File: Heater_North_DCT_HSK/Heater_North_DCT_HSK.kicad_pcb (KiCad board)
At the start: 2 copper layers, 52.1 x 57.1 mm, 8 parts, among them J1 NHB1, J2 NHB2, J3 Heater North

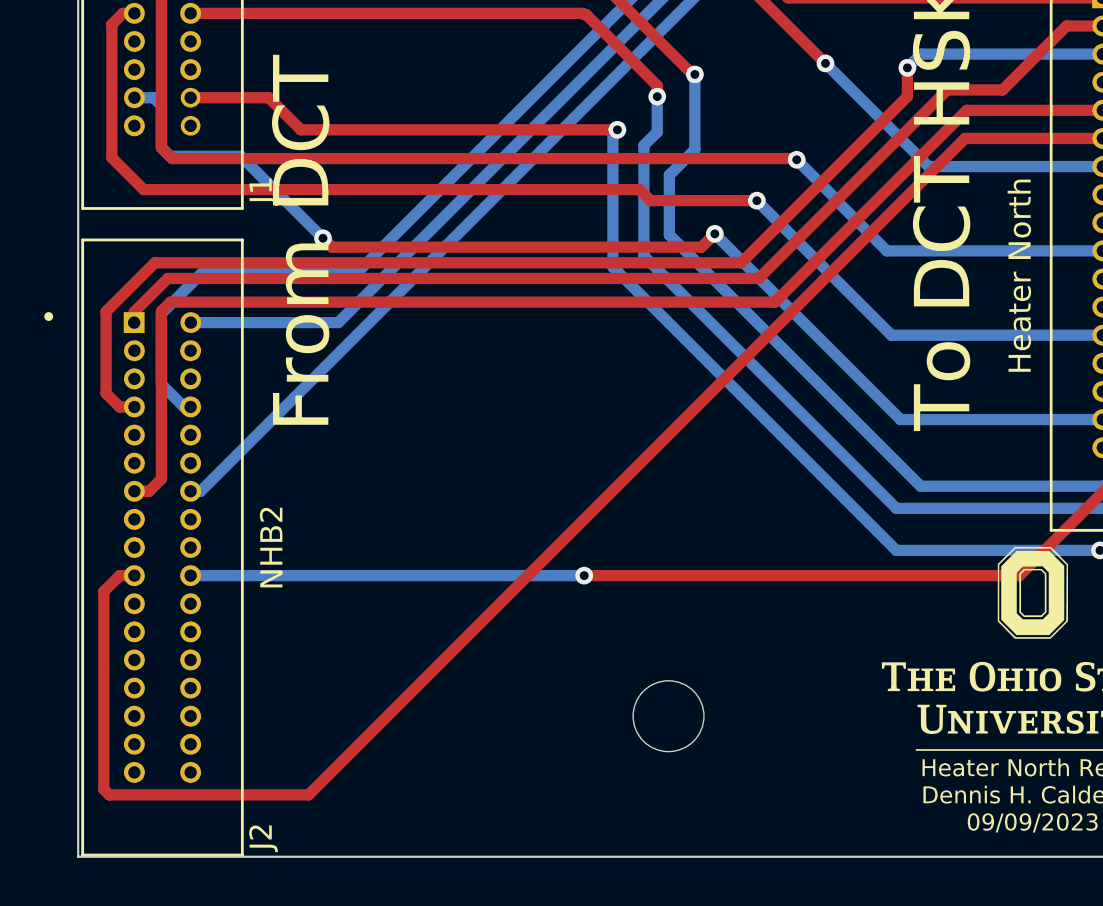
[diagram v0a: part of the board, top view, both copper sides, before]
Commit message: Updated Heater South with correct mapping referencing DCT_Heater_Driver schematic. Updated silscreen on all boards. Generated fabrication files.
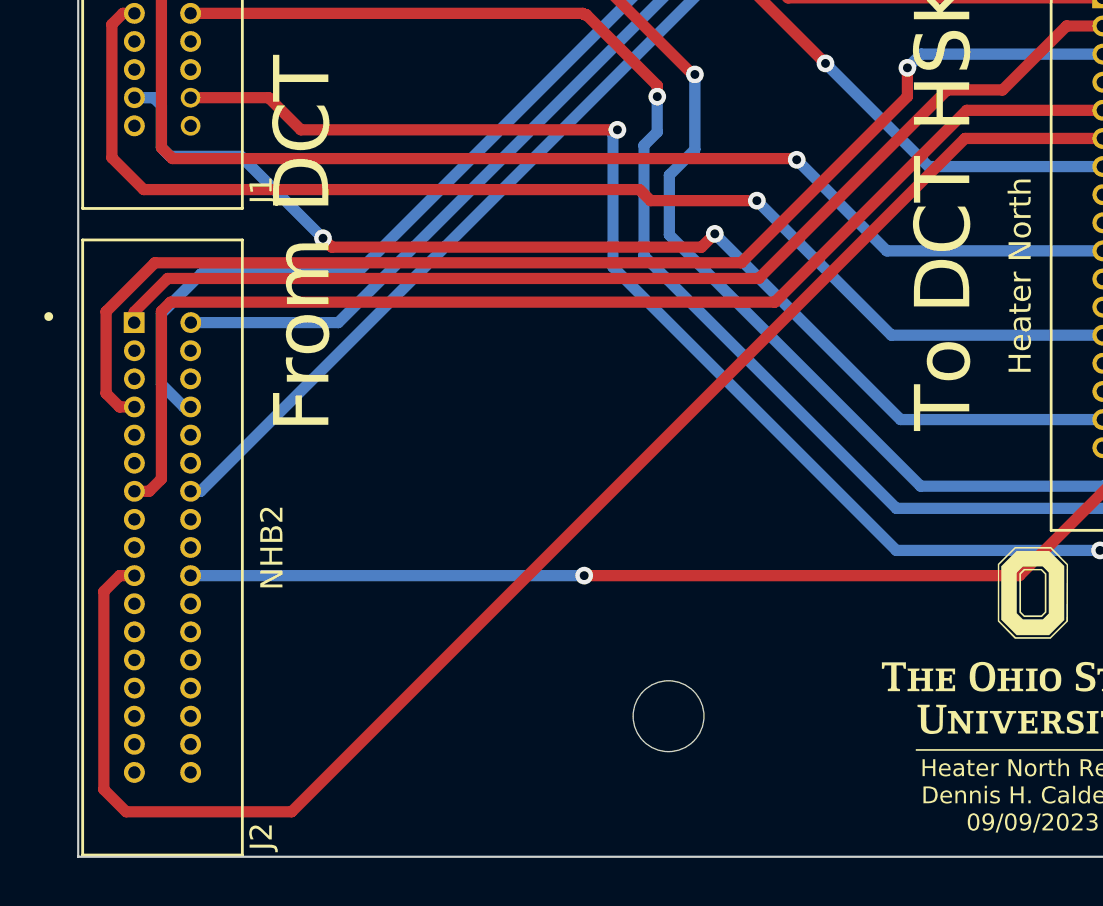
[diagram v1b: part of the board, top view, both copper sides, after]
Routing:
- net /HB2_19: track 68.1 -> 68.8 mm
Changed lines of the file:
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@@
       (outputformat 1)
       (mirror false)
-      (drillshape 1)
+      (drillshape 0)
       (scaleselection 1)
-      (outputdirectory "")
+      (outputdirectory "Fab/Rev_B")
     )
   )
@@
   (segment (start 139 69.6) (end 139 64.2) (width 0.508) (layer "B.Cu") (net 48))
   (segment (start 137.9 63.1) (end 121.5 63.1) (width 0.508) (layer "B.Cu") (net 48))
-  (segment (start 92.6 92.154754) (end 93.314754 91.44) (width 0.508) (layer "F.Cu") (net 53))
-  (segment (start 101.846261 101.346) (end 92.846 101.346) (width 0.508) (layer "F.Cu") (net 53))
-  (segment (start 93.314754 91.44) (end 93.98 91.44) (width 0.508) (layer "F.Cu") (net 53))
+  (segment (start 101.084261 102.108) (end 93.608 102.108) (width 0.508) (layer "F.Cu") (net 53))
   (segment (start 137.73 71.69) (end 131.502261 71.69) (width 0.508) (layer "F.Cu") (net 53))
+  (segment (start 131.502261 71.69) (end 101.084261 102.108) (width 0.508) (layer "F.Cu") (net 53))
+  (segment (start 93.314754 91.44) (end 93.98 91.44) (width 0.508) (layer "F.Cu") (net 53))
+  (segment (start 93.608 102.108) (end 92.6 101.1) (width 0.508) (layer "F.Cu") (net 53))
+  (segment (start 92.6 92.154754) (end 93.314754 91.44) (width 0.508) (layer "F.Cu") (net 53))
   (segment (start 92.6 101.1) (end 92.6 92.154754) (width 0.508) (layer "F.Cu") (net 53))
-  (segment (start 92.846 101.346) (end 92.6 101.1) (width 0.508) (layer "F.Cu") (net 53))
-  (segment (start 131.502261 71.69) (end 101.846261 101.346) (width 0.508) (layer "F.Cu") (net 53))
   (segment (start 139 86.4) (end 139 72.294754) (width 0.508) (layer "F.Cu") (net 54))
   (segment (start 114.3 91.44) (end 133.96 91.44) (width 0.508) (layer "F.Cu") (net 54))

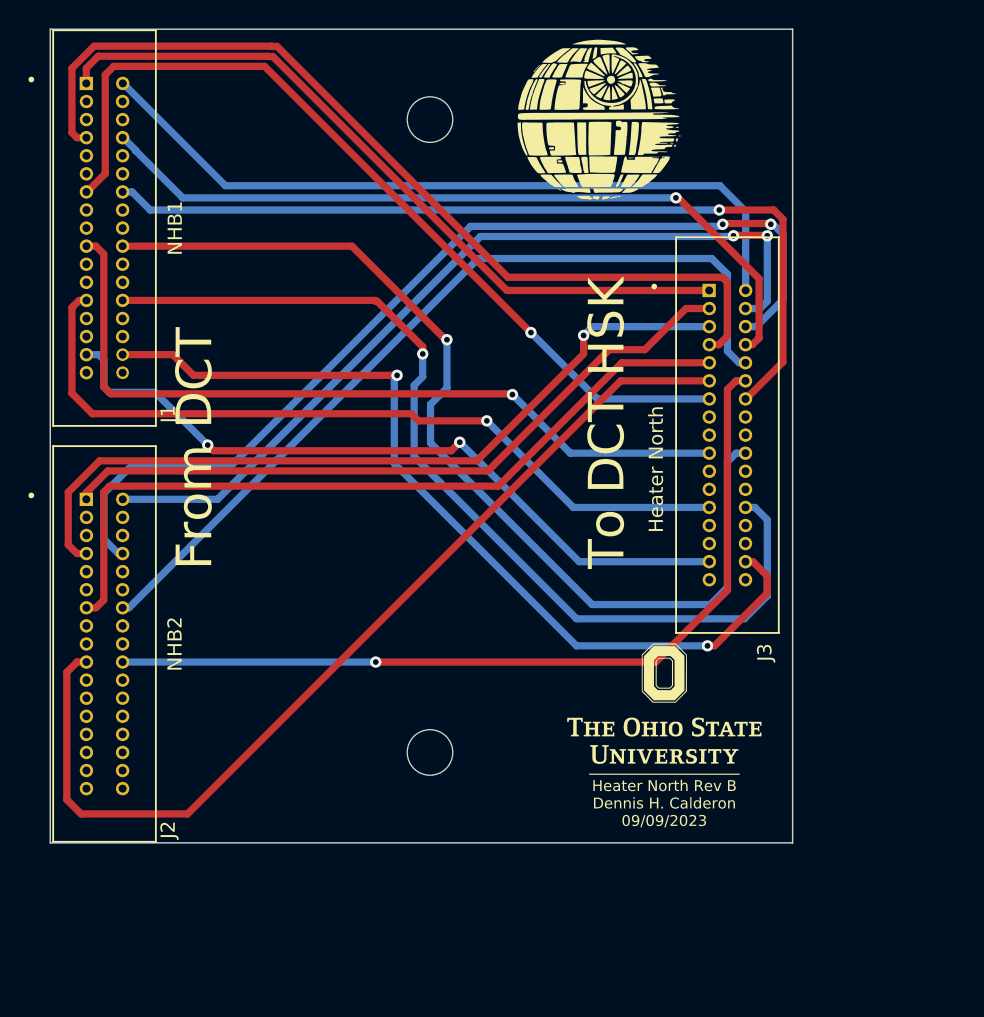
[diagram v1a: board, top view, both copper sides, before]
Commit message: I was working towards fabrication. Chaged the KiCAD violation issues for each PCB to run all tests and make some important silkscreen font bigger. I also edited a few traces and even removed a few vias to make the trace clearance to the edge of the PCBs larger. Need to add the correct centers for the 34-pin connectors on each PCB, rerun traces, and then we should be good.
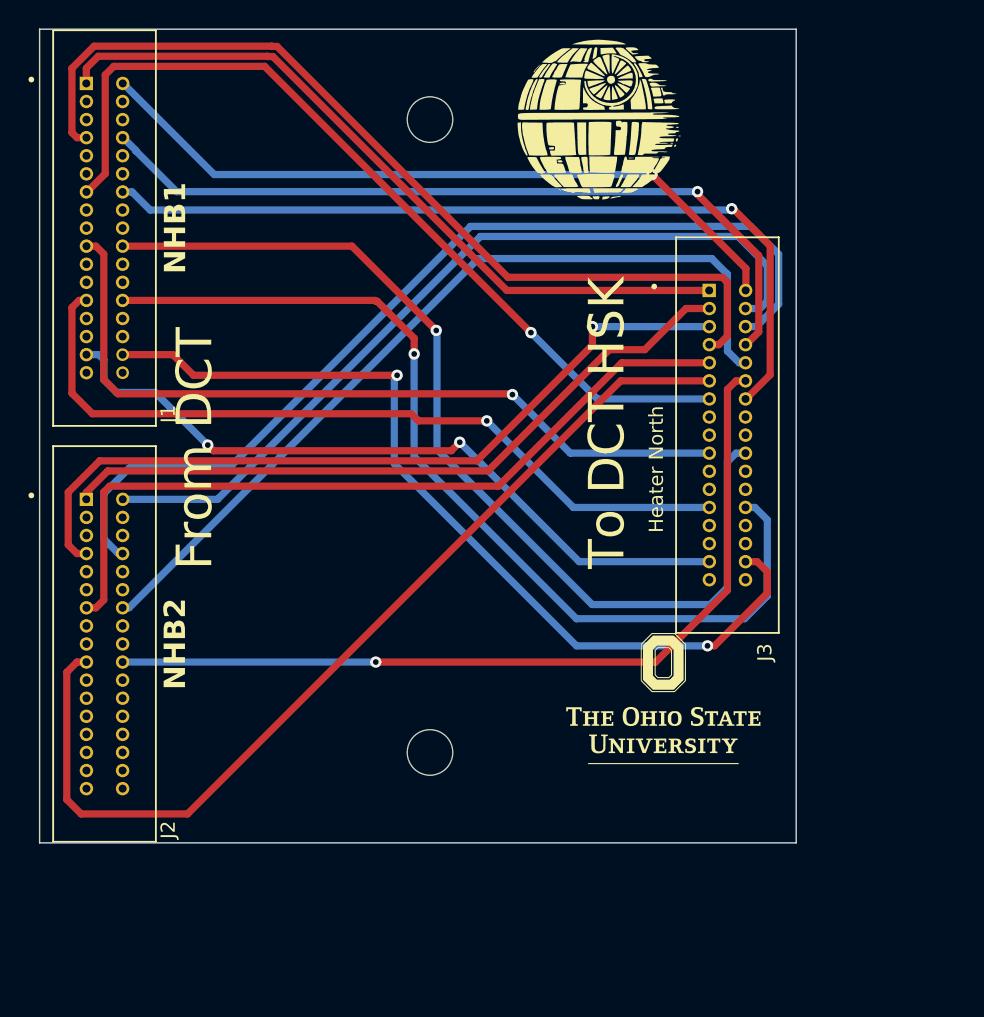
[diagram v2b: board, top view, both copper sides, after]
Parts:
- moved G*** 0.75 mm to (134.5, 94.0)
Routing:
- net /HB1_2: track 53.0 -> 50.7 mm, vias 0 -> 1
- net /HB1_14: track 60.9 -> 58.6 mm
- net /HB2_2: track 59.6 -> 58.0 mm, vias 2 -> 0
- net /HB2_8: track 68.9 -> 67.4 mm, vias 2 -> 0
- net /HB1_20: track 69.6 -> 68.6 mm
- net /HB1_8: track 54.1 -> 54.9 mm
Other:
- board size 52.1 x 57.1 mm -> 53.1 x 57.1 mm

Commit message: Updated Heater and Temp PCBs to board size 2.5in x 2.1in. Updated traces and silkscreens
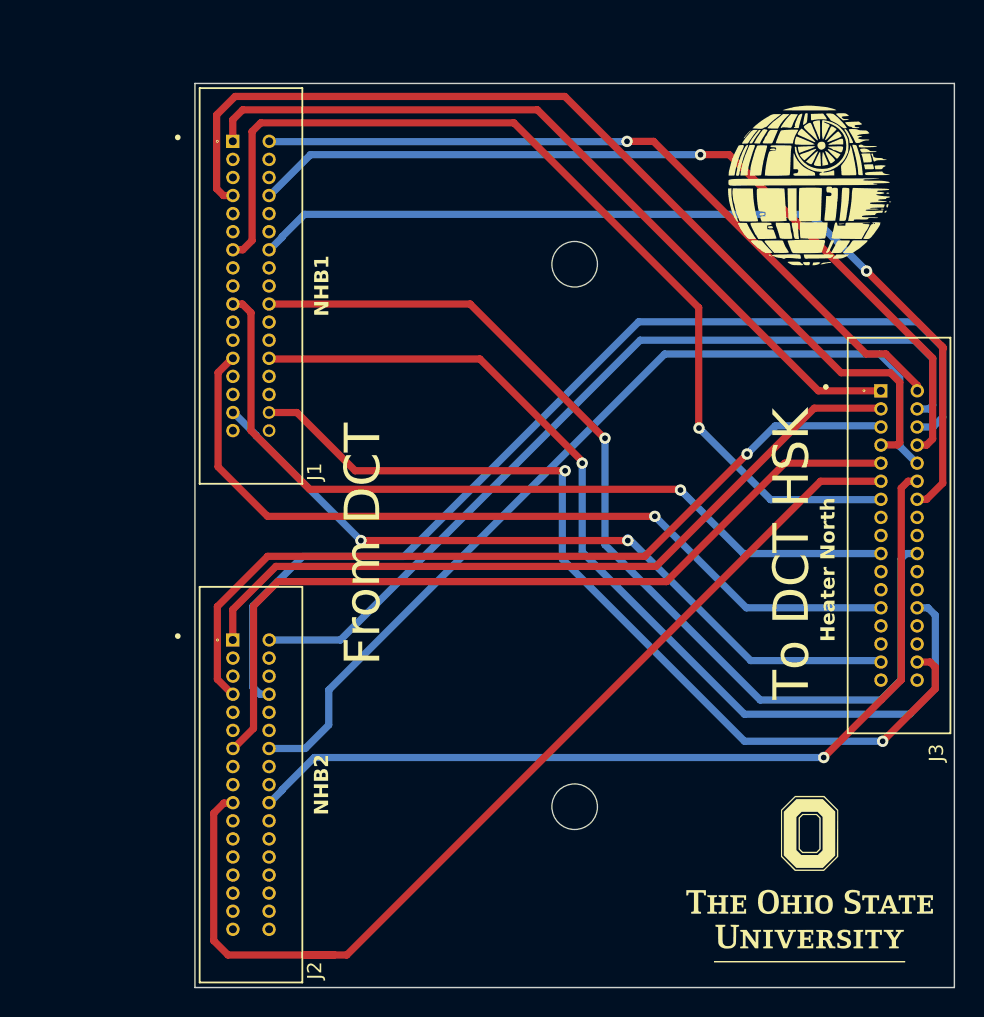
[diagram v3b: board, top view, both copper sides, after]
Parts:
- G***: value LOGO -> Medium OSU; footprint LOGO -> Fun_Logos:Medium OSU
- G***: footprint LOGO -> Fun_Logos:Super Large OSU
- REF**: value MountingHole_3.2mm_M3_DIN965 -> H1
- REF**: value MountingHole_3.2mm_M3_DIN965 -> H2
- moved G*** 16.5 mm to (139.0, 82.5)
- moved G*** 16.3 mm to (144.8, 106.7)
- moved G*** 15.5 mm to (144.8, 58.4)
- moved REF** 14.4 mm to (128.3, 63.5)
- moved J2 14.3 mm to (105.5, 100.1)
- moved J3 14.0 mm to (151.1, 82.5)
- moved J1 11.1 mm to (105.5, 65.0)
- moved REF** 10.9 mm to (128.3, 101.6)
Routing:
- net /HB1_13: track 61.1 -> 69.6 mm
- net /HB1_8: track 54.9 -> 60.7 mm
- net /HB1_14: track 58.6 -> 64.3 mm
- net /HB2_19: track 68.8 -> 73.8 mm
- net /HB2_14: track 60.1 -> 64.6 mm
- net /HB1_7: track 64.5 -> 68.9 mm
- net /HB2_8: track 67.4 -> 71.5 mm
- net /HB2_1: track 49.6 -> 53.5 mm
- net /HB2_13: track 55.3 -> 58.9 mm
- net /HB1_1: track 52.0 -> 55.5 mm
- net /HB1_25: track 55.3 -> 58.7 mm
- net /HB1_19: track 55.0 -> 57.7 mm
- net /HB2_7: track 55.8 -> 58.5 mm
- net /HB2_20: track 60.2 -> 62.8 mm
- net /HB2_2: track 58.0 -> 60.3 mm
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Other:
- board size 53.1 x 57.1 mm -> 53.3 x 63.5 mm
